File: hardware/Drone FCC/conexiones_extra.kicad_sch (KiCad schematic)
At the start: 36 parts, among them J1001 SPI externo, J1002 UARTs externo x 3, J1003 I2C externo x2, J1005 5V 3V3 x2

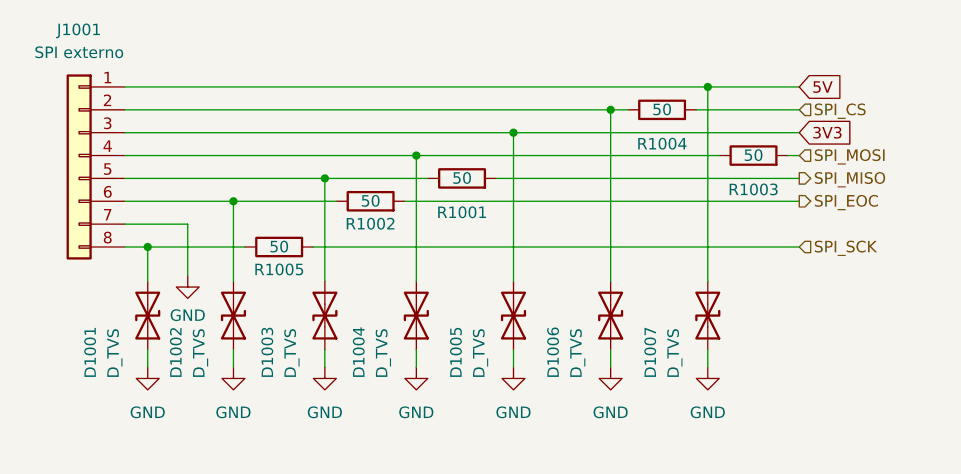
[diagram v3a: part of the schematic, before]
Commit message: moved microSD to top layer. Also transistors for LEDs
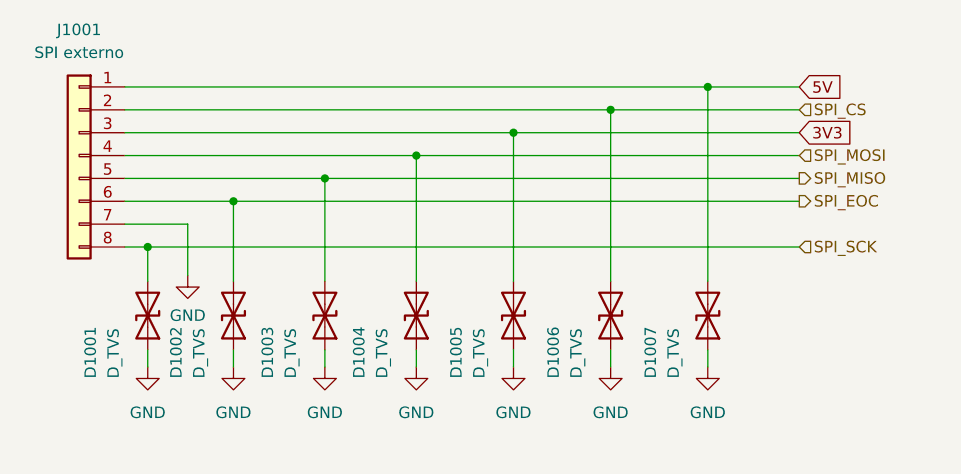
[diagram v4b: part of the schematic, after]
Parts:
- removed R1001, R1002, R1003, R1004, R1005: 50, Resistor_SMD:R_0402_1005Metric_Pad0.72x0.64mm_HandSolder, symbol Device:R
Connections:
- net SPI_CS: now also D1006.2 (A2), J1001.2 (Pin_2)
- net SPI_EOC: now also D1002.2 (A2), J1001.6 (Pin_6)
- net SPI_MISO: now also D1003.2 (A2), J1001.5 (Pin_5)
- net SPI_MOSI: now also D1004.2 (A2), J1001.4 (Pin_4)
- net SPI_SCK: now also D1001.2 (A2), J1001.8 (Pin_8)
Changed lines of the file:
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@@
-    (stroke (width 0) (type default) (color 0 0 0 0))
-  )
-  (wire (pts (xy 78.74 30.48) (xy 80.645 30.48))
     (stroke (width 0) (type default) (color 0 0 0 0))
   )
@@
     (stroke (width 0) (type default) (color 0 0 0 0))
   )
-  (wire (pts (xy 27.305 45.72) (xy 38.1 45.72))
+  (wire (pts (xy 27.305 45.72) (xy 99.695 45.72))
     (stroke (width 0) (type default) (color 0 0 0 0))
   )
@@
     (stroke (width 0) (type default) (color 0 0 0 0))
   )
-  (wire (pts (xy 88.265 30.48) (xy 99.695 30.48))
+  (wire (pts (xy 78.74 30.48) (xy 99.695 30.48))
     (stroke (width 0) (type default) (color 0 0 0 0))
   )
@@
     (stroke (width 0) (type default) (color 0 0 0 0))
   )
-  (wire (pts (xy 66.04 38.1) (xy 99.695 38.1))
-    (stroke (width 0) (type default) (color 0 0 0 0))
-  )
   (wire (pts (xy 30.48 114.935) (xy 30.48 116.84))
     (stroke (width 0) (type default) (color 0 0 0 0))
@@
     (stroke (width 0) (type default) (color 0 0 0 0))
   )
-  (wire (pts (xy 36.83 40.64) (xy 48.26 40.64))
+  (wire (pts (xy 36.83 40.64) (xy 99.695 40.64))
     (stroke (width 0) (type default) (color 0 0 0 0))
   )
@@
     (stroke (width 0) (type default) (color 0 0 0 0))
   )
-  (wire (pts (xy 45.72 45.72) (xy 99.695 45.72))
-    (stroke (width 0) (type default) (color 0 0 0 0))
-  )
   (wire (pts (xy 231.775 36.83) (xy 256.54 36.83))
     (stroke (width 0) (type default) (color 0 0 0 0))
@@
     (stroke (width 0) (type default) (color 0 0 0 0))
   )
-  (wire (pts (xy 55.88 40.64) (xy 99.695 40.64))
-    (stroke (width 0) (type default) (color 0 0 0 0))
-  )
   (wire (pts (xy 46.99 57.15) (xy 46.99 59.055))
     (stroke (width 0) (type default) (color 0 0 0 0))
@@
     (stroke (width 0) (type default) (color 0 0 0 0))
   )
-  (wire (pts (xy 98.425 35.56) (xy 99.695 35.56))
-    (stroke (width 0) (type default) (color 0 0 0 0))
-  )
   (wire (pts (xy 186.69 68.58) (xy 186.69 70.485))
     (stroke (width 0) (type default) (color 0 0 0 0))
@@
     (stroke (width 0) (type default) (color 0 0 0 0))
   )
-  (wire (pts (xy 57.15 35.56) (xy 90.805 35.56))
+  (wire (pts (xy 57.15 35.56) (xy 99.695 35.56))
     (stroke (width 0) (type default) (color 0 0 0 0))
   )
@@
     (stroke (width 0) (type default) (color 0 0 0 0))
   )
-  (wire (pts (xy 46.99 38.1) (xy 58.42 38.1))
+  (wire (pts (xy 46.99 38.1) (xy 99.695 38.1))
     (stroke (width 0) (type default) (color 0 0 0 0))
   )
@@
     (pin "1")
   )
-  (symbol (lib_id "Device:R") (at 41.91 45.72 90) (unit 1)
-    (in_bom yes) (on_board yes)
-    (property "Reference" "R1005" (id 0) (at 41.91 48.26 90))
-    (property "Value" "50" (id 1) (at 41.91 45.72 90))
-    (property "Footprint" "Resistor_SMD:R_0402_1005Metric_Pad0.72x0.64mm_HandSolder" (id 2) (at 41.91 47.498 90)
-      (effects (font (size 1.27 1.27)) hide)
-    )
-    (property "Datasheet" "~" (id 3) (at 41.91 45.72 0)
-      (effects (font (size 1.27 1.27)) hide)
-    )
-    (pin "1")
-    (pin "2")
-  )
   (symbol (lib_id "power:GND") (at 195.58 70.485 0) (unit 1)
     (in_bom yes) (on_board yes) (fields_autoplaced)
@@
     (pin "1")
   )
-  (symbol (lib_id "Device:R") (at 52.07 40.64 90) (unit 1)
-    (in_bom yes) (on_board yes)
-    (property "Reference" "R1002" (id 0) (at 52.07 43.18 90))
-    (property "Value" "50" (id 1) (at 52.07 40.64 90))
-    (property "Footprint" "Resistor_SMD:R_0402_1005Metric_Pad0.72x0.64mm_HandSolder" (id 2) (at 52.07 42.418 90)
-      (effects (font (size 1.27 1.27)) hide)
-    )
-    (property "Datasheet" "~" (id 3) (at 52.07 40.64 0)
-      (effects (font (size 1.27 1.27)) hide)
-    )
-    (pin "1")
-    (pin "2")
-  )
-  (symbol (lib_id "Device:R") (at 94.615 35.56 90) (unit 1)
-    (in_bom yes) (on_board yes)
-    (property "Reference" "R1003" (id 0) (at 94.615 39.37 90))
-    (property "Value" "50" (id 1) (at 94.615 35.56 90))
-    (property "Footprint" "Resistor_SMD:R_0402_1005Metric_Pad0.72x0.64mm_HandSolder" (id 2) (at 94.615 37.338 90)
-      (effects (font (size 1.27 1.27)) hide)
-    )
-    (property "Datasheet" "~" (id 3) (at 94.615 35.56 0)
-      (effects (font (size 1.27 1.27)) hide)
-    )
-    (pin "1")
-    (pin "2")
-  )
   (symbol (lib_id "power:GND") (at 250.19 70.485 0) (unit 1)
     (in_bom yes) (on_board yes) (fields_autoplaced)
@@
     (pin "1")
   )
-  (symbol (lib_id "Device:R") (at 62.23 38.1 90) (unit 1)
-    (in_bom yes) (on_board yes)
-    (property "Reference" "R1001" (id 0) (at 62.23 41.91 90))
-    (property "Value" "50" (id 1) (at 62.23 38.1 90))
-    (property "Footprint" "Resistor_SMD:R_0402_1005Metric_Pad0.72x0.64mm_HandSolder" (id 2) (at 62.23 39.878 90)
-      (effects (font (size 1.27 1.27)) hide)
-    )
-    (property "Datasheet" "~" (id 3) (at 62.23 38.1 0)
-      (effects (font (size 1.27 1.27)) hide)
-    )
-    (pin "1")
-    (pin "2")
-  )
   (symbol (lib_id "Device:D_TVS") (at 241.3 64.77 270) (mirror x) (unit 1)
     (in_bom yes) (on_board yes)
@@
       (effects (font (size 1.27 1.27)) hide)
     )
-    (pin "1")
-    (pin "2")
-  )
-  (symbol (lib_id "Device:R") (at 84.455 30.48 90) (unit 1)
-    (in_bom yes) (on_board yes)
-    (property "Reference" "R1004" (id 0) (at 84.455 34.29 90))
-    (property "Value" "50" (id 1) (at 84.455 30.48 90))
-    (property "Footprint" "Resistor_SMD:R_0402_1005Metric_Pad0.72x0.64mm_HandSolder" (id 2) (at 84.455 32.258 90)
-      (effects (font (size 1.27 1.27)) hide)
-    )
-    (property "Datasheet" "~" (id 3) (at 84.455 30.48 0)
-      (effects (font (size 1.27 1.27)) hide)
-    )

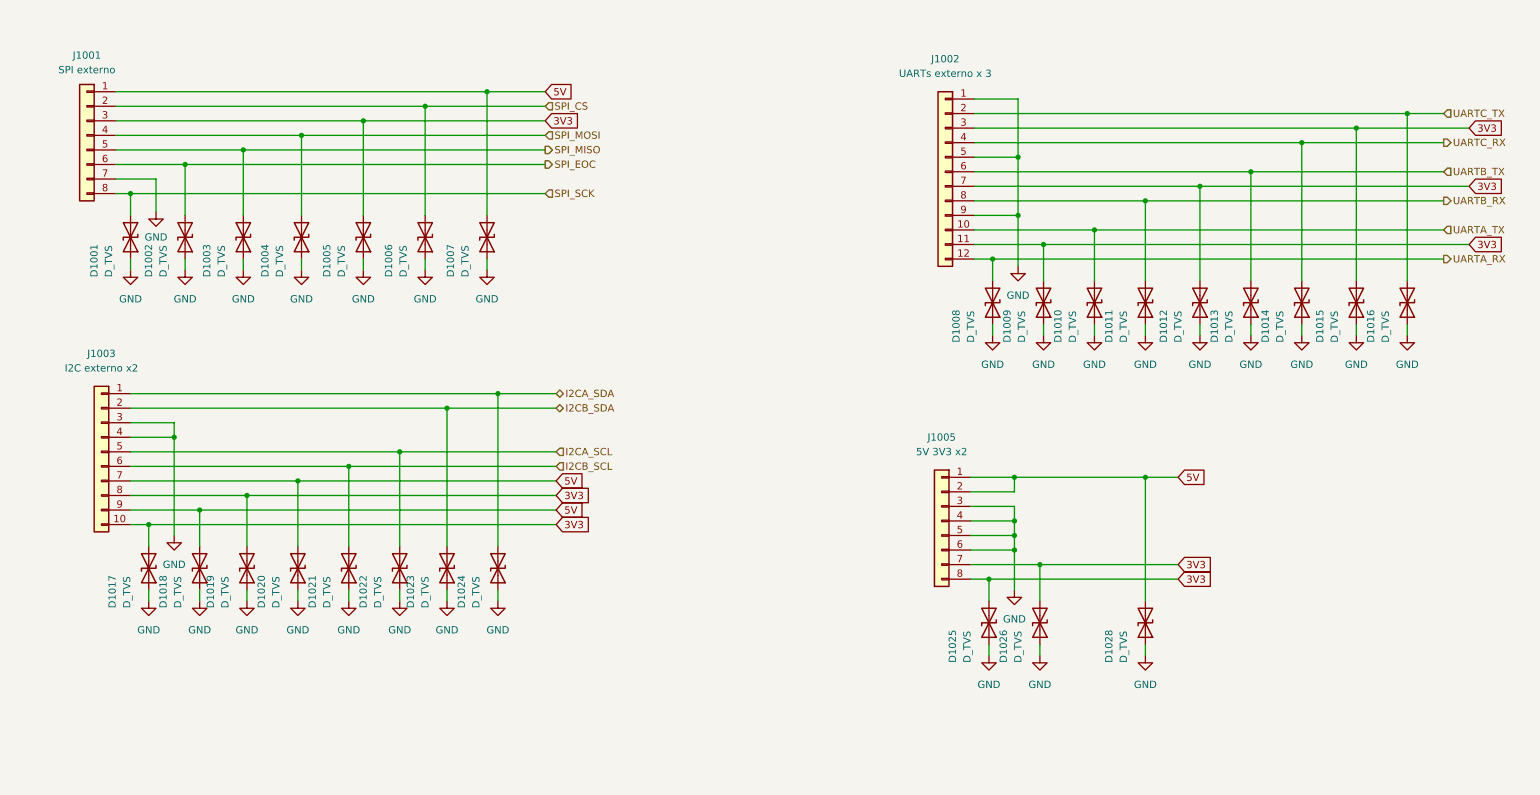
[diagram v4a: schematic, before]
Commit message: removed all the TVS from the PCB and SCH
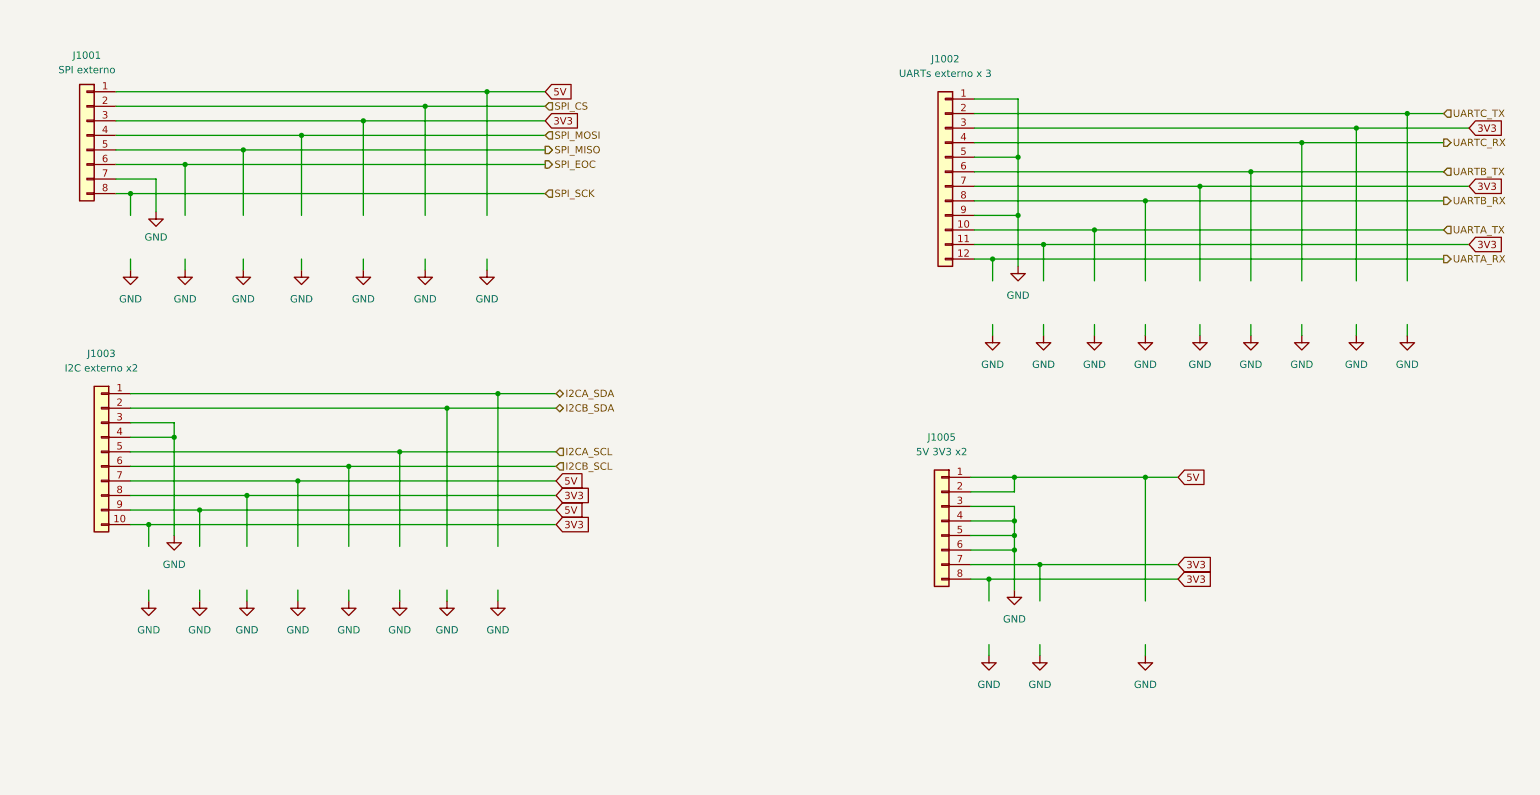
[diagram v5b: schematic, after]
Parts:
- removed D1001, D1002, D1003, D1004, D1005, D1006, D1007, D1008, D1009, D1010, D1011, D1012, D1013, D1014, D1015, D1016, D1017, D1018, D1019, D1020, D1021, D1022, D1023, D1024, D1025, D1026, D1028: D_TVS, Diode_SMD:D_0402_1005Metric_Pad0.77x0.64mm_HandSolder, symbol Device:D_TVS

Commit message: tidying up the schematic
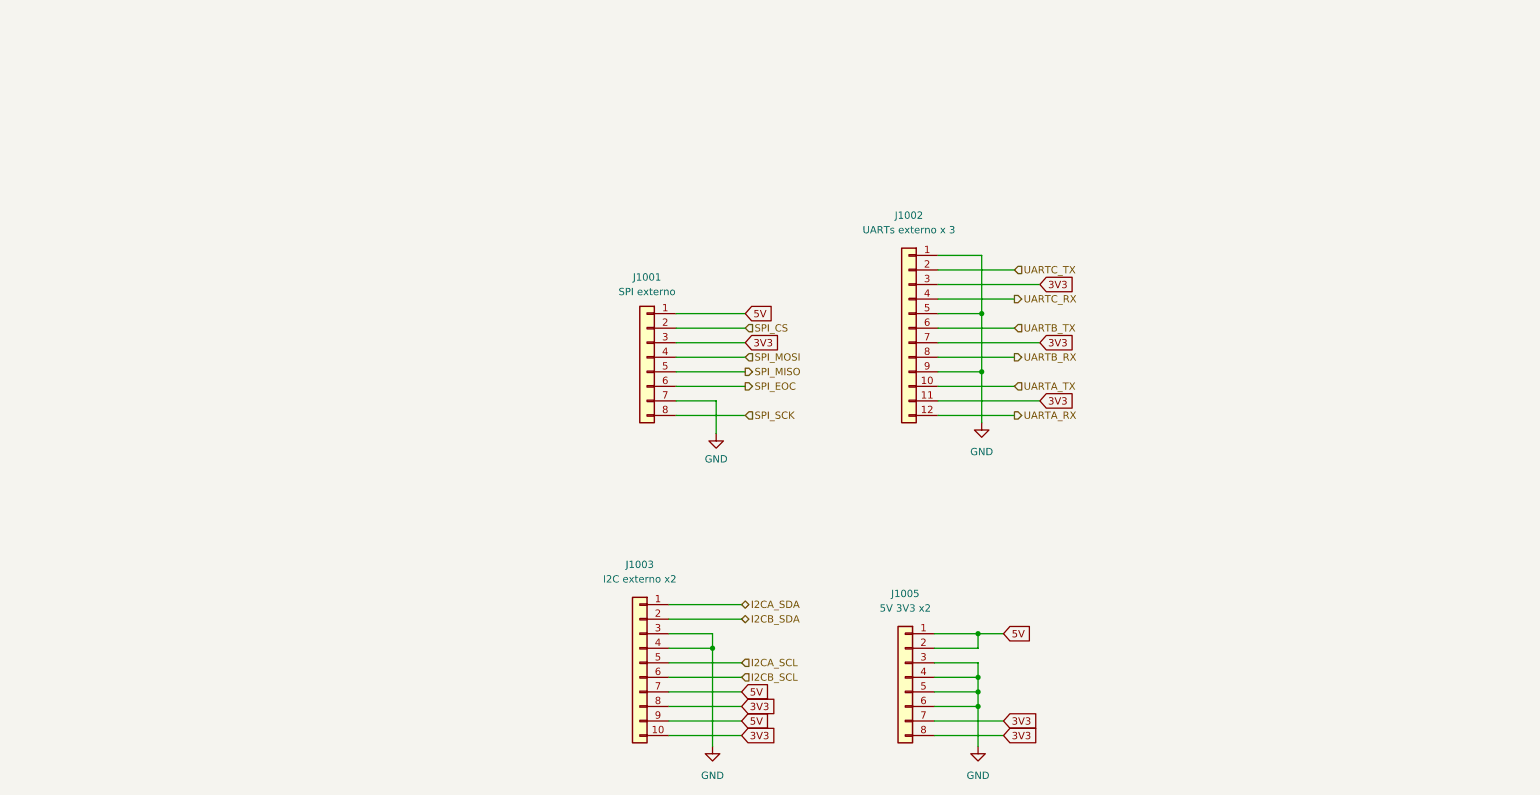
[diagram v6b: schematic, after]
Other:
- moved on the sheet: J1001, J1002, J1003, J1005

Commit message: re enumeation of componentes
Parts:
- renumbered J1003 to J26, J1001 to J27, J1005 to J28, J1002 to J29
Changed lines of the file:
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@@
   (symbol (lib_id "Connector_Generic:Conn_01x10") (at 116.205 127.635 0) (mirror y) (unit 1)
     (in_bom yes) (on_board yes) (fields_autoplaced)
-    (property "Reference" "J1003" (id 0) (at 116.205 110.49 0))
+    (property "Reference" "J26" (id 0) (at 116.205 110.49 0))
     (property "Value" "I2C externo x2" (id 1) (at 116.205 113.03 0))
     (property "Footprint" "Connector_PinHeader_2.54mm:PinHeader_2x05_P2.54mm_Horizontal" (id 2) (at 116.205 127.635 0)
@@
   (symbol (lib_id "power:GND") (at 129.54 87.63 0) (mirror y) (unit 1)
     (in_bom yes) (on_board yes) (fields_autoplaced)
-    (property "Reference" "#PWR0172" (id 0) (at 129.54 93.98 0)
+    (property "Reference" "#PWR081" (id 0) (at 129.54 93.98 0)
       (effects (font (size 1.27 1.27)) hide)
     )
@@
   (symbol (lib_id "Connector_Generic:Conn_01x12") (at 163.195 69.215 0) (mirror y) (unit 1)
     (in_bom yes) (on_board yes) (fields_autoplaced)
-    (property "Reference" "J1002" (id 0) (at 163.195 49.53 0))
+    (property "Reference" "J29" (id 0) (at 163.195 49.53 0))
     (property "Value" "UARTs externo x 3" (id 1) (at 163.195 52.07 0))
     (property "Footprint" "Connector_PinHeader_2.54mm:PinHeader_2x06_P2.54mm_Horizontal" (id 2) (at 163.195 69.215 0)
@@
   (symbol (lib_id "power:GND") (at 175.895 85.725 0) (unit 1)
     (in_bom yes) (on_board yes) (fields_autoplaced)
-    (property "Reference" "#PWR0203" (id 0) (at 175.895 92.075 0)
+    (property "Reference" "#PWR083" (id 0) (at 175.895 92.075 0)
       (effects (font (size 1.27 1.27)) hide)
     )
@@
   (symbol (lib_id "Connector_Generic:Conn_01x08") (at 162.56 130.175 0) (mirror y) (unit 1)
     (in_bom yes) (on_board yes) (fields_autoplaced)
-    (property "Reference" "J1005" (id 0) (at 162.56 115.57 0))
+    (property "Reference" "J28" (id 0) (at 162.56 115.57 0))
     (property "Value" "5V 3V3 x2" (id 1) (at 162.56 118.11 0))
     (property "Footprint" "Connector_PinHeader_2.54mm:PinHeader_2x04_P2.54mm_Horizontal" (id 2) (at 162.56 130.175 0)
@@
   (symbol (lib_id "power:GND") (at 175.26 142.24 0) (unit 1)
     (in_bom yes) (on_board yes) (fields_autoplaced)
-    (property "Reference" "#PWR0174" (id 0) (at 175.26 148.59 0)
+    (property "Reference" "#PWR082" (id 0) (at 175.26 148.59 0)
       (effects (font (size 1.27 1.27)) hide)
     )
@@
   (symbol (lib_id "Connector_Generic:Conn_01x08") (at 117.475 74.295 0) (mirror y) (unit 1)
     (in_bom yes) (on_board yes) (fields_autoplaced)
-    (property "Reference" "J1001" (id 0) (at 117.475 60.325 0))
+    (property "Reference" "J27" (id 0) (at 117.475 60.325 0))
     (property "Value" "SPI externo" (id 1) (at 117.475 62.865 0))
     (property "Footprint" "Connector_PinHeader_2.54mm:PinHeader_2x04_P2.54mm_Horizontal" (id 2) (at 117.475 74.295 0)
@@
   (symbol (lib_id "power:GND") (at 128.905 142.24 0) (unit 1)
     (in_bom yes) (on_board yes) (fields_autoplaced)
-    (property "Reference" "#PWR0206" (id 0) (at 128.905 148.59 0)
+    (property "Reference" "#PWR080" (id 0) (at 128.905 148.59 0)
       (effects (font (size 1.27 1.27)) hide)
     )

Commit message: moved external SPI tracks to TOP layer. Moved external I2C pull ups to TOP layer
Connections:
- net SPI_CS: now also J27.6 (Pin_6); no longer J27.2 (Pin_2)
- net SPI_EOC: now also J27.8 (Pin_8); no longer J27.6 (Pin_6)
- net SPI_MISO: now also J27.4 (Pin_4); no longer J27.5 (Pin_5)
- net SPI_MOSI: now also J27.2 (Pin_2); no longer J27.4 (Pin_4)
- net SPI_SCK: now also J27.5 (Pin_5); no longer J27.8 (Pin_8)
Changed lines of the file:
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@@
     (effects (font (size 1.27 1.27)) (justify left))
   )
-  (hierarchical_label "SPI_MOSI" (shape input) (at 134.62 74.295 0)
+  (hierarchical_label "SPI_MOSI" (shape input) (at 134.62 69.215 0)
     (effects (font (size 1.27 1.27)) (justify left))
   )
-  (hierarchical_label "SPI_EOC" (shape output) (at 134.62 79.375 0)
+  (hierarchical_label "SPI_EOC" (shape output) (at 134.62 84.455 0)
     (effects (font (size 1.27 1.27)) (justify left))
   )
@@
     (effects (font (size 1.27 1.27)) (justify left))
   )
-  (hierarchical_label "SPI_CS" (shape input) (at 134.62 69.215 0)
+  (hierarchical_label "SPI_CS" (shape input) (at 134.62 79.375 0)
     (effects (font (size 1.27 1.27)) (justify left))
   )
@@
     (effects (font (size 1.27 1.27)) (justify left))
   )
-  (hierarchical_label "SPI_MISO" (shape output) (at 134.62 76.835 0)
+  (hierarchical_label "SPI_MISO" (shape output) (at 134.62 74.295 0)
     (effects (font (size 1.27 1.27)) (justify left))
   )
-  (hierarchical_label "SPI_SCK" (shape input) (at 134.62 84.455 0)
+  (hierarchical_label "SPI_SCK" (shape input) (at 134.62 76.835 0)
     (effects (font (size 1.27 1.27)) (justify left))
   )
